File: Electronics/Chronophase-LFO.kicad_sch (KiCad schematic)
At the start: 43 parts, among them J1 CLK In, J7 BP_Inv_Out, J8 UP_Out, J9 BP_Out, U3 TL072, U4 TL072

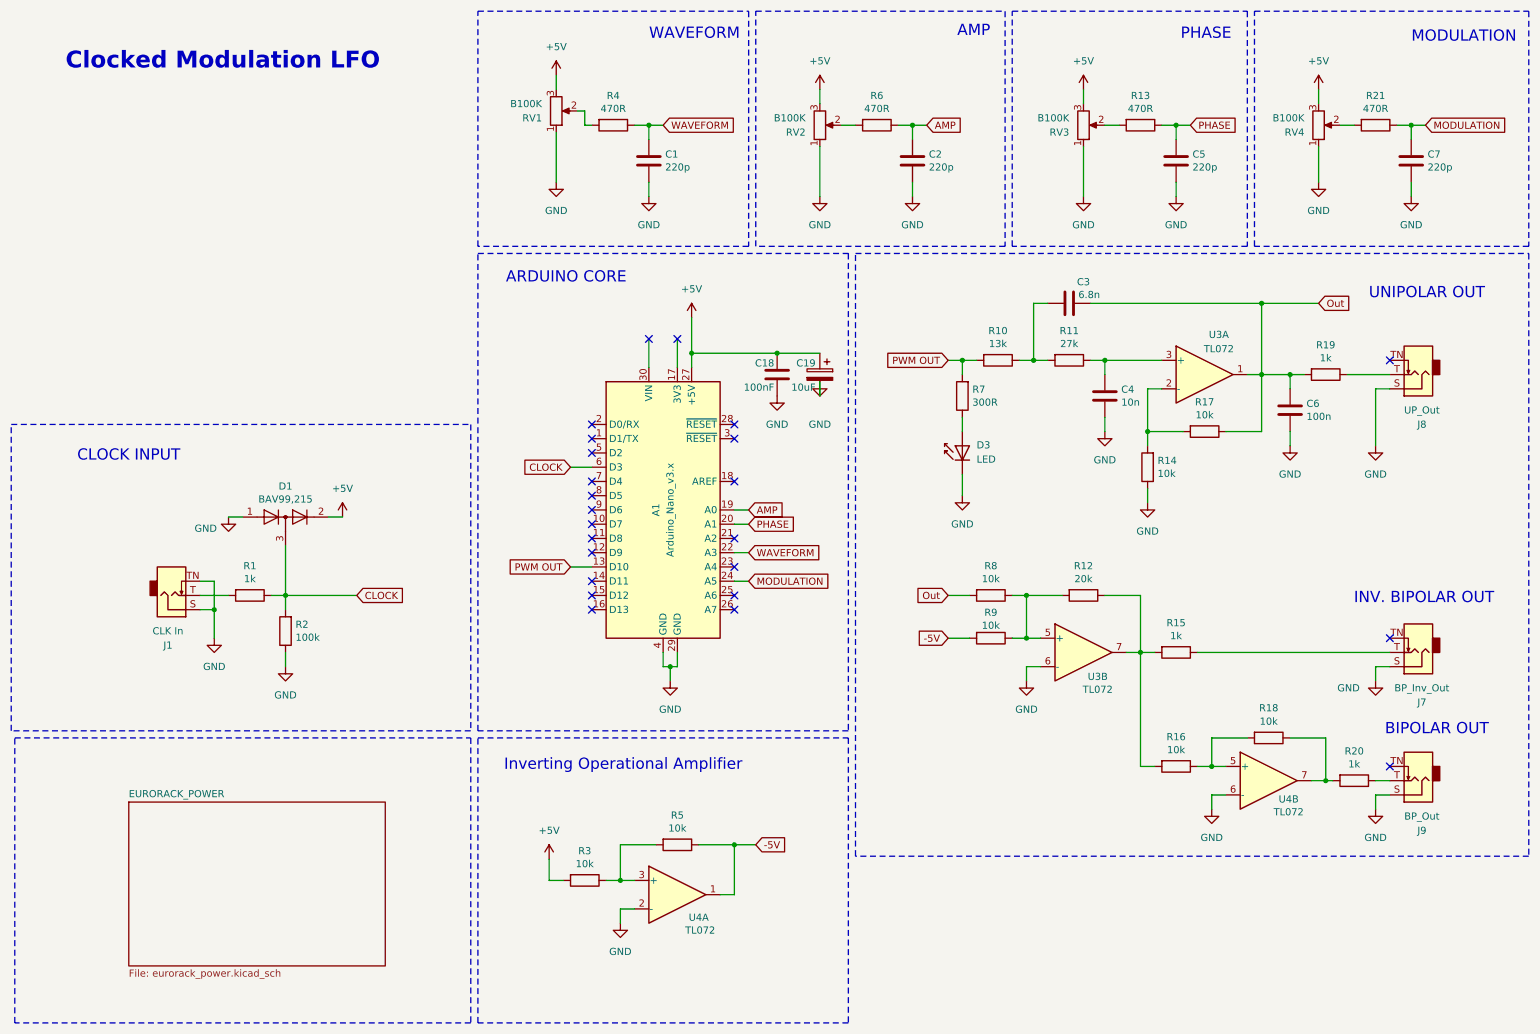
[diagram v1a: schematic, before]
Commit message: fix: swapping the inputs of the opamps
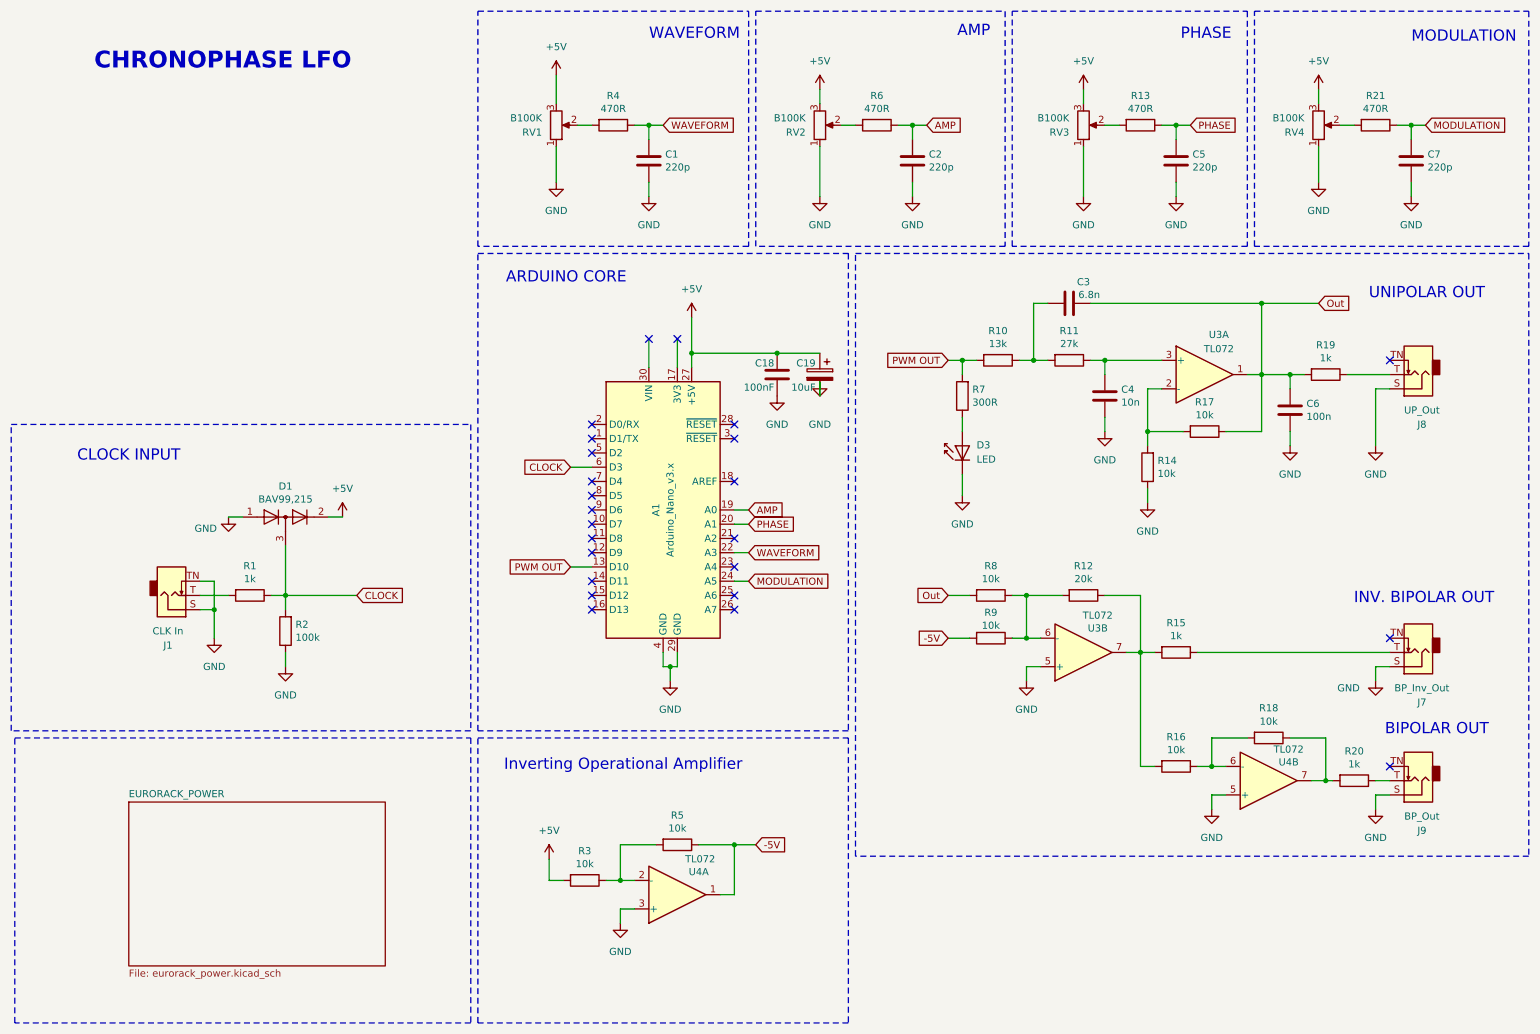
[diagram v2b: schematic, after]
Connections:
- net GND: now also U3.5 (+), U4.3 (+), U4.5 (+); no longer U3.6 (-), U4.2 (-), U4.6 (-)
- net at R3.1, R5.2: now also U4.2 (-); no longer U4.3 (+)
- net at R12.2, R8.1, R9.1: now also U3.6 (-); no longer U3.5 (+)
- net at R16.1, R18.2: now also U4.6 (-); no longer U4.5 (+)
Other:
- note added: "CHRONOPHASE LFO"
- note removed: "Clocked Modulation LFO"
- moved on the sheet: RV1
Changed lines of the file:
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@@
 	(title_block
 		(title "Chronophase LFO")
-		(date "2026-04-01")
-		(rev "v1.0")
+		(date "2026-04-17")
+		(rev "v1.1")
 		(company "© Dirty Dream – Nathanael Noir")
 	)
@@
 		)
 	)
-	(text "Clocked Modulation LFO"
+	(text "CHRONOPHASE LFO "
 		(exclude_from_sim no)
 		(at 51.054 22.86 0)
@@
 	(wire
 		(pts
-			(xy 115.57 34.29) (xy 116.84 34.29)
-		)
-		(stroke
-			(width 0)
-			(type default)
-		)
-	)
-	(wire
-		(pts
 			(xy 246.38 66.04) (xy 236.22 66.04)
 		)
@@
 	(wire
 		(pts
-			(xy 110.49 25.4) (xy 110.49 27.94)
+			(xy 110.49 25.4) (xy 110.49 30.48)
 		)
 		(stroke
@@
 	(wire
 		(pts
-			(xy 115.57 31.75) (xy 114.3 31.75)
+			(xy 114.3 34.29) (xy 116.84 34.29)
 		)
 		(stroke
@@
 	(wire
 		(pts
-			(xy 115.57 34.29) (xy 115.57 31.75)
-		)
-		(stroke
-			(width 0)
-			(type default)
-		)
-	)
-	(wire
-		(pts
 			(xy 124.46 173.99) (xy 121.92 173.99)
 		)
@@
 	(wire
 		(pts
-			(xy 110.49 35.56) (xy 110.49 44.45)
+			(xy 110.49 38.1) (xy 110.49 44.45)
 		)
 		(stroke
@@
 		(lib_id "Amplifier_Operational:TL072")
 		(at 204.47 128.27 0)
+		(mirror x)
 		(unit 2)
 		(body_style 1)
@@
 		(dnp no)
 		(property "Reference" "U3"
-			(at 207.01 132.588 0)
+			(at 207.01 123.952 0)
 			(show_name no)
 			(do_not_autoplace no)
@@
 		)
 		(property "Value" "TL072"
-			(at 207.01 134.874 0)
+			(at 207.01 121.666 0)
 			(show_name no)
 			(do_not_autoplace no)
@@
 		(lib_id "Amplifier_Operational:TL072")
 		(at 237.49 151.13 0)
+		(mirror x)
 		(unit 2)
 		(body_style 1)
@@
 		(dnp no)
 		(property "Reference" "U4"
-			(at 241.046 154.432 0)
+			(at 241.046 147.828 0)
 			(show_name no)
 			(do_not_autoplace no)
@@
 		)
 		(property "Value" "TL072"
-			(at 241.046 156.718 0)
+			(at 241.046 145.542 0)
 			(show_name no)
 			(do_not_autoplace no)
@@
 		(lib_id "Amplifier_Operational:TL072")
 		(at 132.08 171.45 0)
+		(mirror x)
 		(unit 1)
 		(body_style 1)
@@
 		(dnp no)
 		(property "Reference" "U4"
-			(at 135.89 175.514 0)
+			(at 135.89 167.386 0)
 			(show_name no)
 			(do_not_autoplace no)
@@
 		)
 		(property "Value" "TL072"
-			(at 136.144 177.8 0)
+			(at 136.144 165.1 0)
 			(show_name no)
 			(do_not_autoplace no)
@@
 	(symbol
 		(lib_id "Device:R_Potentiometer")
-		(at 110.49 31.75 0)
+		(at 110.49 34.29 0)
 		(mirror x)
 		(unit 1)
@@
 		(dnp no)
 		(property "Reference" "RV1"
-			(at 107.95 33.0201 0)
+			(at 107.95 35.5601 0)
 			(show_name no)
 			(do_not_autoplace no)
@@
 		)
 		(property "Value" "B100K"
-			(at 107.95 30.4801 0)
+			(at 107.95 33.0201 0)
 			(show_name no)
 			(do_not_autoplace no)
@@
 		)
 		(property "Footprint" "Eurorack:Potentiometer_Alpha_RD901F_Vertical_Alt"
-			(at 110.49 31.75 0)
+			(at 110.49 34.29 0)
 			(hide yes)
 			(show_name no)
@@
 		)
 		(property "Datasheet" ""
-			(at 110.49 31.75 0)
+			(at 110.49 34.29 0)
 			(hide yes)
 			(show_name no)
@@
 		)
 		(property "Description" "Potentiometer"
-			(at 110.49 31.75 0)
+			(at 110.49 34.29 0)
 			(hide yes)
 			(show_name no)
